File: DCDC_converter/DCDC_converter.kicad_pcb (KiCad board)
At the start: 4 copper layers, 50 x 20 mm, 33 parts, among them J1 Conn_01x02_Pin, J2 Conn_01x02_Pin, J3 Conn_01x02_Pin, J4 Conn_01x02_Pin, U1 MP2491C

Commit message: Final version of DC/DC module
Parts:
- added J5: Conn_01x03_Pin, Connector_PinHeader_2.54mm:PinHeader_1x03_P2.54mm_Vertical, F.Cu at (85.4, 60.0)
- added J6: Conn_01x02_Pin, Connector_PinHeader_2.54mm:PinHeader_1x02_P2.54mm_Vertical, F.Cu at (89.4, 66.3)
- moved REF** 20.5 mm to (86.5, 68.5)
- moved REF** 17.4 mm to (55.5, 51.5)
- moved J2 14.1 mm to (52.5, 53.6), turned to 0 degrees
- moved J4 13.8 mm to (88.1, 52.4)
- moved J1 12.2 mm to (52.5, 63.8), turned to 0 degrees
- moved C2 8.50 mm to (56.4, 58.7)
- moved R6 8.50 mm to (63.1, 53.6)
- moved C10 8.50 mm to (80.3, 66.5)
- moved C11 8.50 mm to (80.3, 68.5)
- moved C12 8.50 mm to (80.2, 51.7)
- moved C13 8.50 mm to (80.2, 53.6)
- moved C3 8.50 mm to (58.3, 58.7)
- moved C5 8.50 mm to (62.0, 58.7)
- moved C7 8.50 mm to (63.5, 61.4)
- moved C8 8.50 mm to (70.7, 57.3)
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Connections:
- J3 pad 1: +5V -> Net-(J3-Pin_1)
- J3 pad 2: +5V -> Net-(J3-Pin_1)
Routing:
- net +5V: vias 10 -> 8
- net Net-(J5-Pin_3): vias 0 -> 7
- net Net-(J3-Pin_1): vias 0 -> 6
- net GND: vias 64 -> 42
- net +24V: vias 37 -> 26
- added copper zone on B.Cu, net Net-(J3-Pin_1)
- added copper zone on F.Cu, net Net-(J3-Pin_1)
- added copper zone on B.Cu, net Net-(J5-Pin_3)
- added copper zone on F.Cu, net Net-(J5-Pin_3)
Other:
- board size 50 x 20 mm -> 42 x 20 mm
- board text added: "O1"
- board text added: "O2"
- board text removed: "OUT"

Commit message: Flipping the headers to bottom side
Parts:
- J1, J2, J3, J4, J6: moved to B.Cu
- turned J1 to 180 degrees
- turned J2 to 180 degrees
- turned J3 to 180 degrees
- turned J6 to 180 degrees

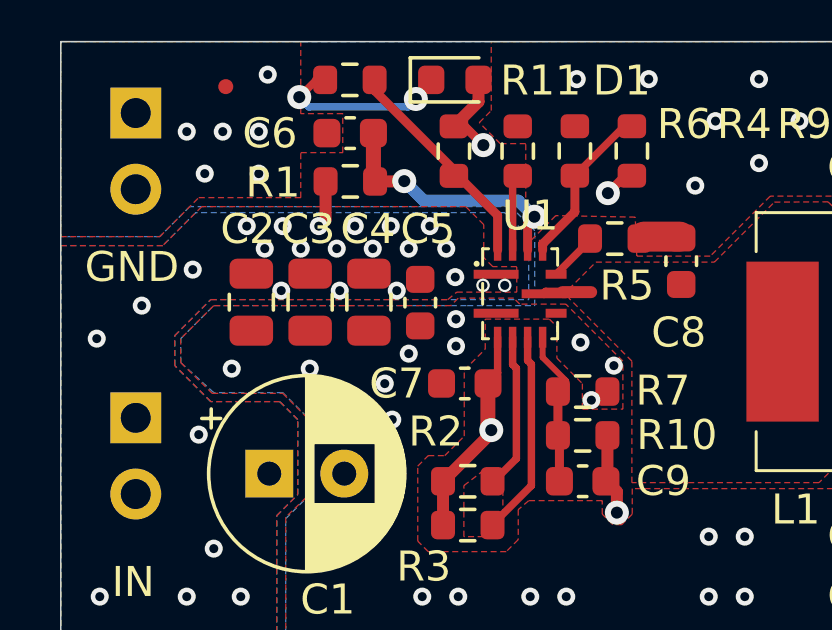
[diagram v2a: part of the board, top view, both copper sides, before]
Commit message: Bigger gaps between +24V and GND
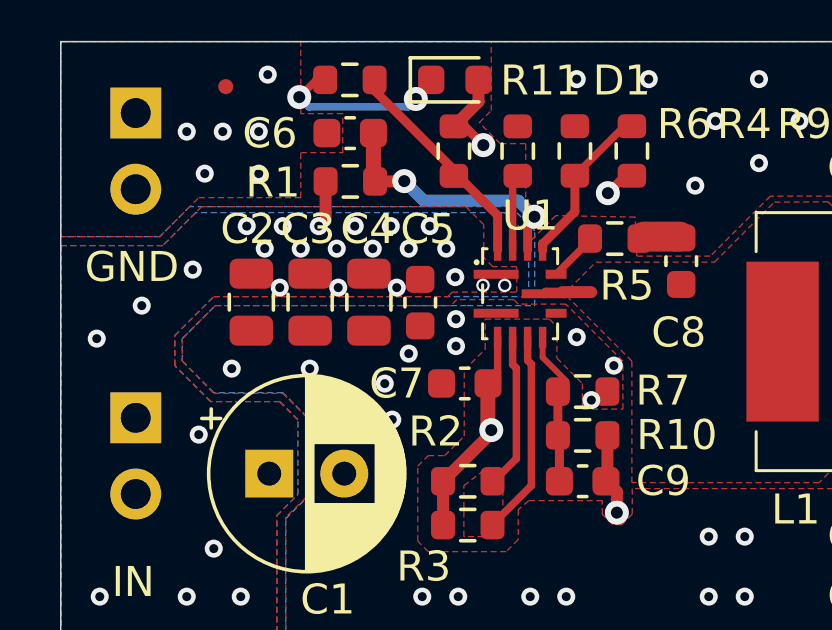
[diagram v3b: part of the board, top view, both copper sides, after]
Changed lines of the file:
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@@
 		(fp_line
 			(start -1.25 -1.5)
-			(end -1.25 -0.95)
+			(end -1.25 -1)
 			(stroke
 				(width 0.1)
@@
 		(fp_line
 			(start -1.25 -1.5)
-			(end -1.05 -1.5)
+			(end -1.1 -1.5)
 			(stroke
 				(width 0.1)
@@
 		)
 		(fp_line
-			(start -1.25 -0.35)
-			(end -1.25 0.35)
+			(start -1.25 -0.3)
+			(end -1.25 0.3)
 			(stroke
 				(width 0.1)
@@
 		)
 		(fp_line
-			(start -1.25 0.95)
+			(start -1.25 1)
 			(end -1.25 1.5)
 			(stroke
@@
 		(fp_line
 			(start -1.25 1.5)
-			(end -1.05 1.5)
+			(end -1.1 1.5)
 			(stroke
 				(width 0.1)
@@
 		)
 		(fp_line
-			(start 1.05 -1.5)
+			(start 1.1 -1.5)
 			(end 1.25 -1.5)
 			(stroke
@@
 		)
 		(fp_line
-			(start 1.05 1.5)
+			(start 1.1 1.5)
 			(end 1.25 1.5)
 			(stroke
@@
 		(fp_line
 			(start 1.25 -1.5)
-			(end 1.25 -0.95)
+			(end 1.25 -1)
 			(stroke
 				(width 0.1)
@@
 		)
 		(fp_line
-			(start 1.25 0.95)
+			(start 1.25 1)
 			(end 1.25 1.5)
 			(stroke
@@
 		)
 		(fp_circle
-			(center -1.45 -1)
-			(end -1.4 -1)
+			(center -1.45 -1.05)
+			(end -1.4 -1.05)
 			(stroke
 				(width 0.1)
@@
 	)
 	(via
-		(at 67.325 60.025)
+		(at 67.2 59.85)
 		(size 0.6)
 		(drill 0.3)
@@
 	)
 	(via
-		(at 61.2 58.3)
+		(at 61.2 58.2)
 		(size 0.6)
 		(drill 0.3)
@@
 	)
 	(via
-		(at 59.3 58.3)
+		(at 59.25 58.2)
 		(size 0.6)
 		(drill 0.3)
@@
 	)
 	(via
-		(at 57.35 58.3)
+		(at 57.3 58.2)
 		(size 0.6)
 		(drill 0.3)
@@
 			(pts
 				(xy 50 70) (xy 57.2 70) (xy 57.2 65.8) (xy 57.9 65.1) (xy 57.9 62.6) (xy 57.3 62) (xy 55 62) (xy 53.8 60.8)
-				(xy 53.8 59.8) (xy 55 58.6) (xy 62.9 58.6) (xy 63.2 58.35) (xy 65.2 58.35) (xy 65.2 57.5) (xy 64.4 57.5)
+				(xy 53.8 59.8) (xy 55.1 58.5) (xy 62.9 58.5) (xy 63.05 58.35) (xy 65.2 58.35) (xy 65.2 57.5) (xy 64.4 57.5)
 				(xy 64.1 57.2) (xy 64.1 56.1) (xy 63.5 55.5) (xy 54.7 55.5) (xy 53.4 56.8) (xy 50 56.8)
 			)
@@
 		(polygon
 			(pts
-				(xy 68.7375 62.25) (xy 68.7375 60.65) (xy 66.8375 58.75) (xy 65.3 58.75) (xy 65.1 58.55) (xy 63.25 58.55)
-				(xy 63 58.8) (xy 55.1 58.8) (xy 54 59.9) (xy 54 60.7) (xy 55.05 61.725) (xy 57.4 61.725) (xy 58.175 62.5)
-				(xy 58.175 65.2) (xy 57.5 65.85) (xy 57.5 70) (xy 80.15 70) (xy 80.15 65.15) (xy 79.9 64.9) (xy 69.05 64.9)
-				(xy 69.05 65.75) (xy 68.7 66.1) (xy 68.4 66.1) (xy 68.05 65.75) (xy 68.05 65.3) (xy 65.6 65.3) (xy 65.25 65.6)
-				(xy 65.25 66.6) (xy 64.85 67) (xy 62.25 67) (xy 61.9 66.65) (xy 61.9 64.15) (xy 62.25 63.8) (xy 62.8 63.8)
-				(xy 63.45 63.15) (xy 63.45 60.95) (xy 64.15 60.25) (xy 64.15 59.25) (xy 66.2875 59.25) (xy 66.5375 59.5)
-				(xy 66.5375 60.55) (xy 67.3875 61.4) (xy 67.3875 62.25)
+				(xy 68.7375 62.25) (xy 68.7375 60.65) (xy 66.8375 58.75) (xy 65.25 58.75) (xy 65.1 58.6) (xy 63.2 58.6)
+				(xy 63 58.8) (xy 55.15 58.8) (xy 54.05 59.9) (xy 54.05 60.65) (xy 55.1 61.725) (xy 57.4 61.725)
+				(xy 58.175 62.5) (xy 58.175 65.2) (xy 57.5 65.85) (xy 57.5 70) (xy 80.15 70) (xy 80.15 65.15) (xy 79.9 64.9)
+				(xy 69.05 64.9) (xy 69.05 65.75) (xy 68.7 66.1) (xy 68.4 66.1) (xy 68.05 65.75) (xy 68.05 65.3)
+				(xy 65.6 65.3) (xy 65.25 65.6) (xy 65.25 66.6) (xy 64.85 67) (xy 62.25 67) (xy 61.9 66.65) (xy 61.9 64.15)
+				(xy 62.25 63.8) (xy 62.8 63.8) (xy 63.45 63.15) (xy 63.45 60.95) (xy 64.15 60.25) (xy 64.15 59.25)
+				(xy 66.2875 59.25) (xy 66.5375 59.5) (xy 66.5375 60.55) (xy 67.3875 61.4) (xy 67.3875 62.25)
 			)
 		)
@@
 			(pts
 				(xy 50 70) (xy 57.2 70) (xy 57.2 65.8) (xy 57.9 65.1) (xy 57.9 62.6) (xy 57.3 62) (xy 55 62) (xy 53.8 60.8)
-				(xy 53.8 59.8) (xy 55 58.6) (xy 65.6 58.6) (xy 65.6 56.5) (xy 64.8 55.7) (xy 54.5 55.7) (xy 53.4 56.8)
+				(xy 53.8 59.8) (xy 55.1 58.5) (xy 65.6 58.5) (xy 65.6 56.5) (xy 64.8 55.7) (xy 54.5 55.7) (xy 53.4 56.8)
 				(xy 50 56.8)
 			)
@@
 			(pts
 				(xy 77.5 55.2) (xy 76.7 56) (xy 76.7 63.7) (xy 77.5 64.5) (xy 79.3 64.5) (xy 80.1 65.2) (xy 80.1 70)
-				(xy 57.5 70) (xy 57.5 65.9) (xy 58.2 65.2) (xy 58.2 62.5) (xy 57.4 61.7) (xy 55.1 61.7) (xy 54 60.7)
-				(xy 54 59.9) (xy 55.1 58.8) (xy 61.4 58.8) (xy 63.55 58.8) (xy 65.8 58.8) (xy 65.8 56.3) (xy 65 55.5)
+				(xy 57.5 70) (xy 57.5 65.9) (xy 58.2 65.2) (xy 58.2 62.5) (xy 57.4 61.7) (xy 55.1 61.7) (xy 54.05 60.65)
+				(xy 54.05 59.9) (xy 55.15 58.8) (xy 61.4 58.8) (xy 63.55 58.8) (xy 65.8 58.8) (xy 65.8 56.3) (xy 65 55.5)
 				(xy 54.3 55.5) (xy 53.3 56.5) (xy 50 56.5) (xy 50 50) (xy 57.4 50) (xy 80.1 50) (xy 80.1 54.9) (xy 79.8 55.2)
 			)

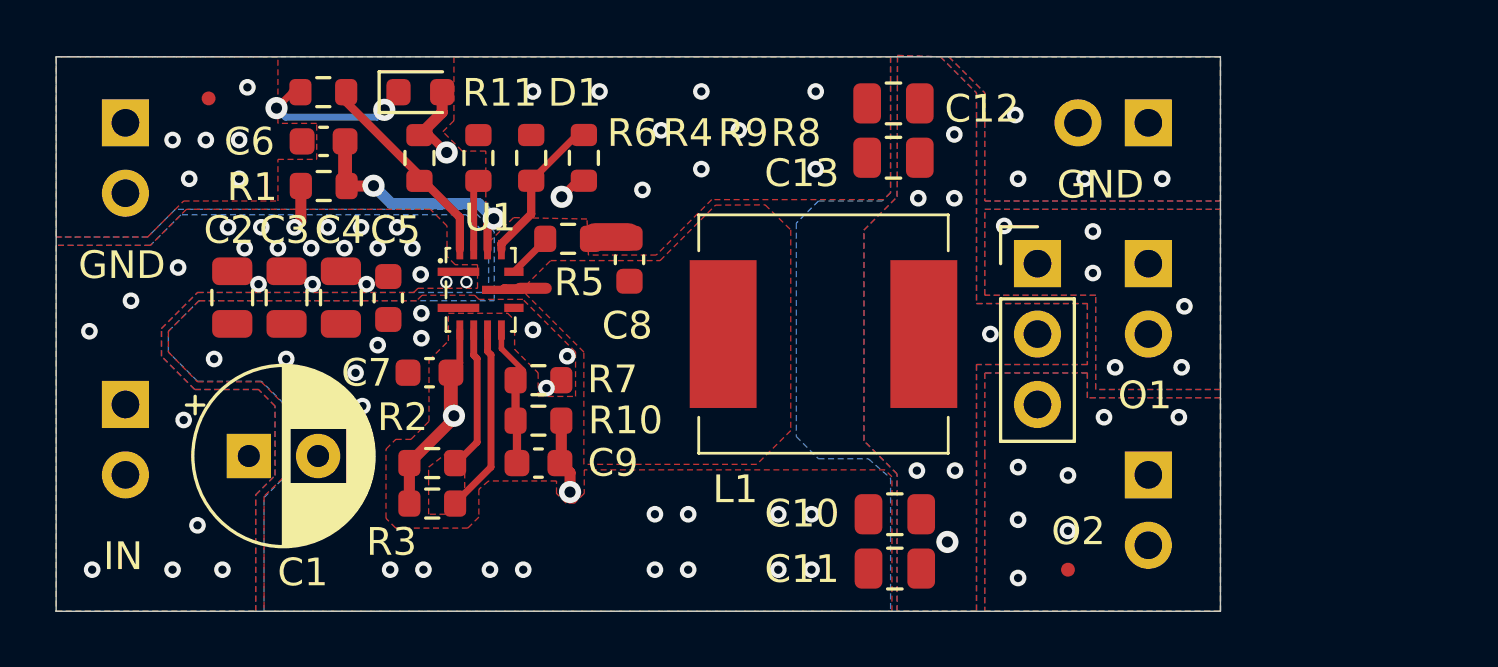
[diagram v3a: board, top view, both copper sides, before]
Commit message: PCB shortened to final measurements
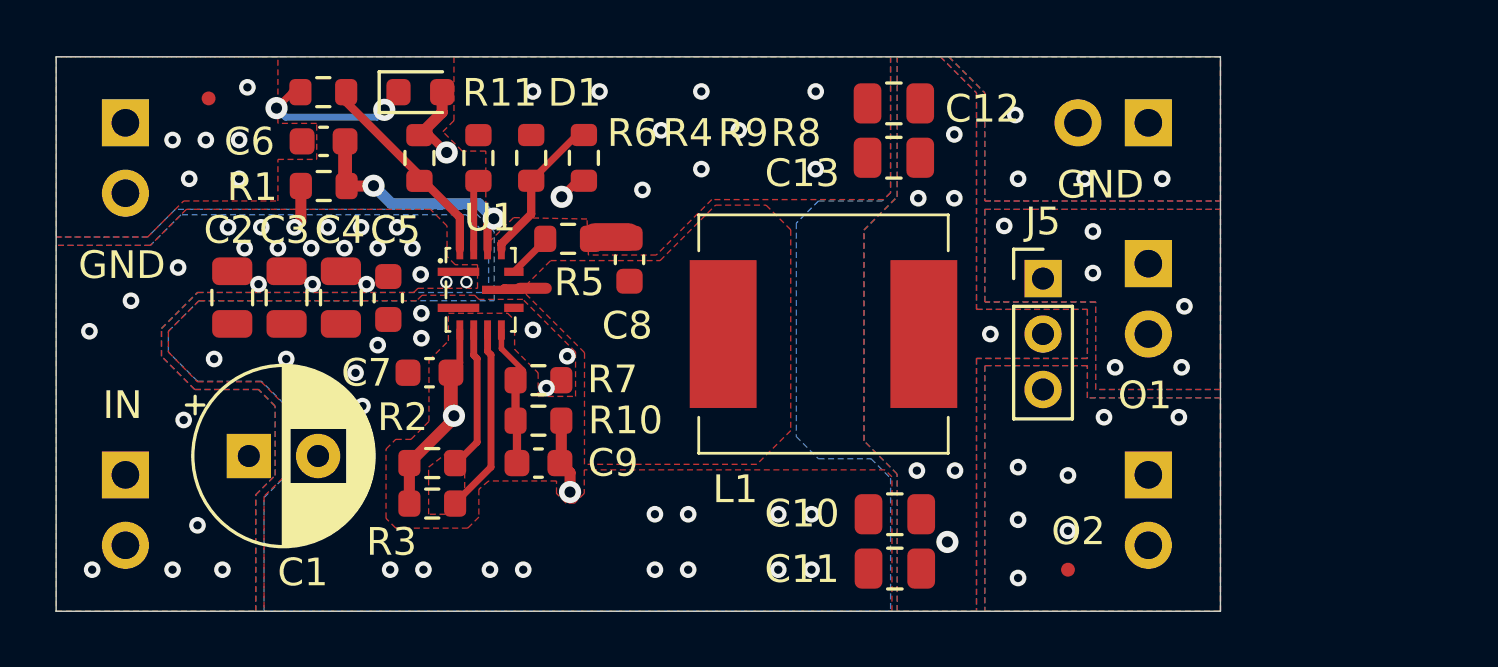
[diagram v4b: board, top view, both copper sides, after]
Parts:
- J5: footprint Connector_PinHeader_2.54mm:PinHeader_1x03_P2.54mm_Vertical -> Connector_PinHeader_2.00mm:PinHeader_1x03_P2.00mm_Vertical
- moved J1 2.54 mm to (52.5, 66.3)
- moved J5 0.20 mm to (85.6, 60.0)
